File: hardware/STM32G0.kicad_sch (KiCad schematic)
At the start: 15 parts, among them T1 TP_+3V3, U1 STM32G0C1KCTxN

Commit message: reorganization of project folders acording to templates
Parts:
- added D8: LED_Debug, LED_SMD:LED_01005_0402Metric_Pad0.57x0.30mm_HandSolder, symbol Device:LED_Small
- added R7: 1k, Resistor_SMD:R_0603_1608Metric_Pad0.98x0.95mm_HandSolder, symbol Device:R_Small
- D1, D2, D3: footprint (none) -> LED_SMD:LED_01005_0402Metric_Pad0.57x0.30mm_HandSolder
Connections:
- net +3V3: now also R7.2
- net LED.ACT: now reaches U1.17 (PB15)
- net LED.ACT: now also D8.1 (K)
- net DET: now reaches U1.29 (PD3)
- new net: D8.2 (A), R7.1
- no-connect marks 14 -> 12
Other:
- moved on the sheet: D1, D2, D3, R2, R3, R4, R5, U1

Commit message: added missing files
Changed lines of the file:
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@@
 		)
 	)
-	(label "NRST"
+	(label "RST"
 		(at 128.27 78.74 180)
 		(effects

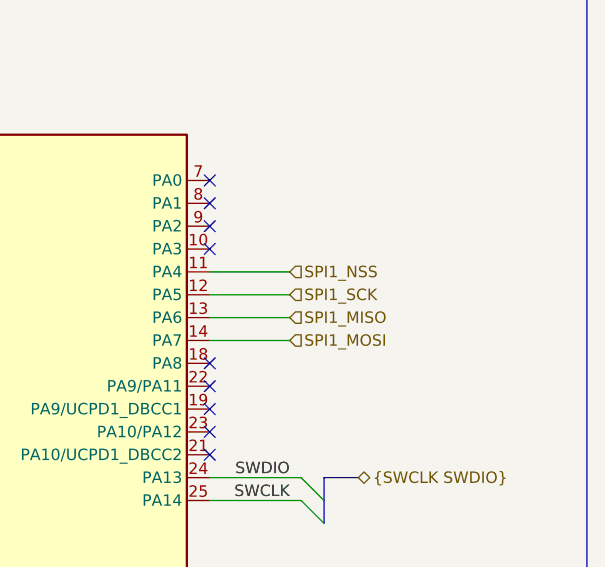
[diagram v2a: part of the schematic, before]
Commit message: reorganize SPI signals into bus
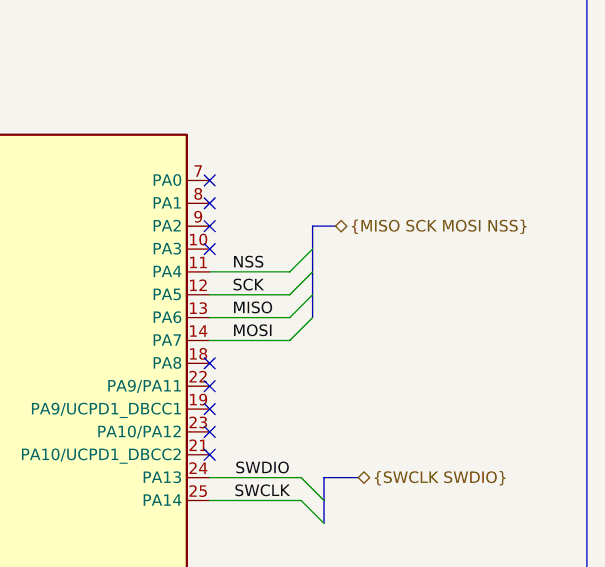
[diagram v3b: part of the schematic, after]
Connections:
- net SPI1_MISO renamed MISO
- net SPI1_MOSI renamed MOSI
- net SPI1_NSS renamed NSS
- net SPI1_SCK renamed SCK
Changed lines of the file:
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@@
+	)
+	(bus_entry
+		(at 200.66 91.44)
+		(size -2.54 2.54)
+		(stroke
+			(width 0)
+			(type default)
+		)
 	)
 	(bus_entry
@@
 		)
 	)
+	(bus_entry
+		(at 200.66 93.98)
+		(size -2.54 2.54)
+		(stroke
+			(width 0)
+			(type default)
+		)
+	)
+	(bus_entry
+		(at 200.66 86.36)
+		(size -2.54 2.54)
+		(stroke
+			(width 0)
+			(type default)
+		)
+	)
+	(bus_entry
+		(at 200.66 88.9)
+		(size -2.54 2.54)
+		(stroke
+			(width 0)
+			(type default)
+		)
+	)
 	(wire
 		(pts
@@
 		)
 	)
+	(bus
+		(pts
+			(xy 200.66 83.82) (xy 203.2 83.82)
+		)
+		(stroke
+			(width 0)
+			(type default)
+		)
+	)
 	(wire
 		(pts
@@
 		)
 	)
+	(bus
+		(pts
+			(xy 200.66 83.82) (xy 200.66 88.9)
+		)
+		(stroke
+			(width 0)
+			(type default)
+		)
+	)
 	(wire
 		(pts
 			(xy 95.25 50.8) (xy 100.33 50.8)
+		)
+		(stroke
+			(width 0)
+			(type default)
+		)
+	)
+	(bus
+		(pts
+			(xy 200.66 88.9) (xy 200.66 93.98)
 		)
 		(stroke
@@
 		)
 	)
+	(label "SCK"
+		(at 191.77 91.44 0)
+		(effects
+			(font
+				(size 1.27 1.27)
+			)
+			(justify left bottom)
+		)
+	)
+	(label "MOSI"
+		(at 191.77 96.52 0)
+		(effects
+			(font
+				(size 1.27 1.27)
+			)
+			(justify left bottom)
+		)
+	)
 	(label "STM_VCC"
 		(at 163.83 50.8 180)
@@
 		)
 	)
+	(label "MISO"
+		(at 191.77 93.98 0)
+		(effects
+			(font
+				(size 1.27 1.27)
+			)
+			(justify left bottom)
+		)
+	)
 	(label "LED.OK"
 		(at 119.38 116.84 0)
@@
 		)
 	)
+	(label "NSS"
+		(at 191.77 88.9 0)
+		(effects
+			(font
+				(size 1.27 1.27)
+			)
+			(justify left bottom)
+		)
+	)
 	(label "LED.WRN"
 		(at 119.38 96.52 0)
@@
 			)
 			(justify left bottom)
-		)
-	)
-	(hierarchical_label "SPI1_MOSI"
-		(shape input)
-		(at 198.12 96.52 0)
-		(effects
-			(font
-				(size 1.27 1.27)
-			)
-			(justify left)
-		)
-	)
-	(hierarchical_label "SPI1_SCK"
-		(shape input)
-		(at 198.12 91.44 0)
-		(effects
-			(font
-				(size 1.27 1.27)
-			)
-			(justify left)
 		)
 	)
@@
 		)
 	)
-	(hierarchical_label "SPI1_NSS"
-		(shape input)
-		(at 198.12 88.9 0)
-		(effects
-			(font
-				(size 1.27 1.27)
-			)
-			(justify left)
-		)
-	)
 	(hierarchical_label "STBY_CAN"
 		(shape output)
@@
 		)
 	)
-	(hierarchical_label "SPI1_MISO"
-		(shape input)
-		(at 198.12 93.98 0)
-		(effects
-			(font
-				(size 1.27 1.27)
-			)
-			(justify left)
-		)
-	)
 	(hierarchical_label "USART.RX"
 		(shape input)
@@
 		)
 	)
+	(hierarchical_label "{MISO SCK MOSI NSS}"
+		(shape bidirectional)
+		(at 203.2 83.82 0)
+		(effects
+			(font
+				(size 1.27 1.27)
+			)
+			(justify left)
+		)
+	)

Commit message: changed pcb layout
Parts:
- D1, D2, D3, D8: footprint LED_SMD:LED_01005_0402Metric_Pad0.57x0.30mm_HandSolder -> LED_SMD:LED_0603_1608Metric_Pad1.05x0.95mm_HandSolder
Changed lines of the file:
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@@
 			)
 		)
-		(property "Footprint" "LED_SMD:LED_01005_0402Metric_Pad0.57x0.30mm_HandSolder"
+		(property "Footprint" "LED_SMD:LED_0603_1608Metric_Pad1.05x0.95mm_HandSolder"
 			(at 85.09 116.84 90)
 			(hide yes)
@@
 			)
 		)
-		(property "Footprint" "LED_SMD:LED_01005_0402Metric_Pad0.57x0.30mm_HandSolder"
+		(property "Footprint" "LED_SMD:LED_0603_1608Metric_Pad1.05x0.95mm_HandSolder"
 			(at 85.09 137.16 90)
 			(hide yes)
@@
 			)
 		)
-		(property "Footprint" "LED_SMD:LED_01005_0402Metric_Pad0.57x0.30mm_HandSolder"
+		(property "Footprint" "LED_SMD:LED_0603_1608Metric_Pad1.05x0.95mm_HandSolder"
 			(at 85.09 142.24 90)
 			(hide yes)
@@
 			)
 		)
-		(property "Footprint" "LED_SMD:LED_01005_0402Metric_Pad0.57x0.30mm_HandSolder"
+		(property "Footprint" "LED_SMD:LED_0603_1608Metric_Pad1.05x0.95mm_HandSolder"
 			(at 85.09 127 90)
 			(hide yes)

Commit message: fixed routing issues
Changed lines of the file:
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@@
 		)
 		(pin "30"
+			(alternate "USART1_TX")
 		)
 		(pin "31"
+			(alternate "USART1_RX")
 		)
 		(pin "8"
 		)
 		(pin "14"
+			(alternate "SPI1_MOSI")
 		)
 		(pin "23"
@@
 		)
 		(pin "24"
+			(alternate "SYS_SWDIO")
 		)
 		(pin "13"
+			(alternate "SPI1_MISO")
 		)
 		(pin "5"
@@
 		)
 		(pin "11"
+			(alternate "SPI1_NSS")
 		)
 		(pin "32"
 		)
 		(pin "26"
+			(alternate "FDCAN1_RX")
 		)
 		(pin "16"
 		)
 		(pin "12"
+			(alternate "SPI1_SCK")
 		)
 		(pin "10"
 		)
 		(pin "6"
+			(alternate "LPUART2_RTS")
 		)
 		(pin "9"
@@
 		)
 		(pin "25"
+			(alternate "SYS_SWCLK")
 		)
 		(pin "27"
+			(alternate "FDCAN1_TX")
 		)
 		(pin "22"
